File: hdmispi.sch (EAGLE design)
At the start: 3 parts

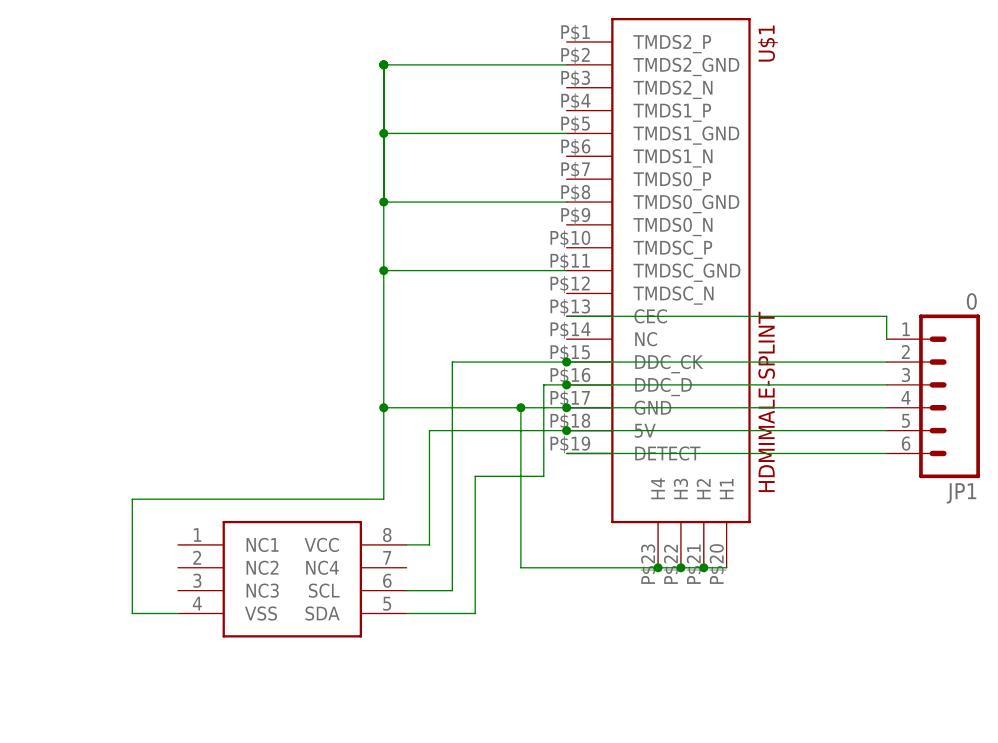
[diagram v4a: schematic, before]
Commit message: added micro hdmi header and revised board to match. note different pinout!!!
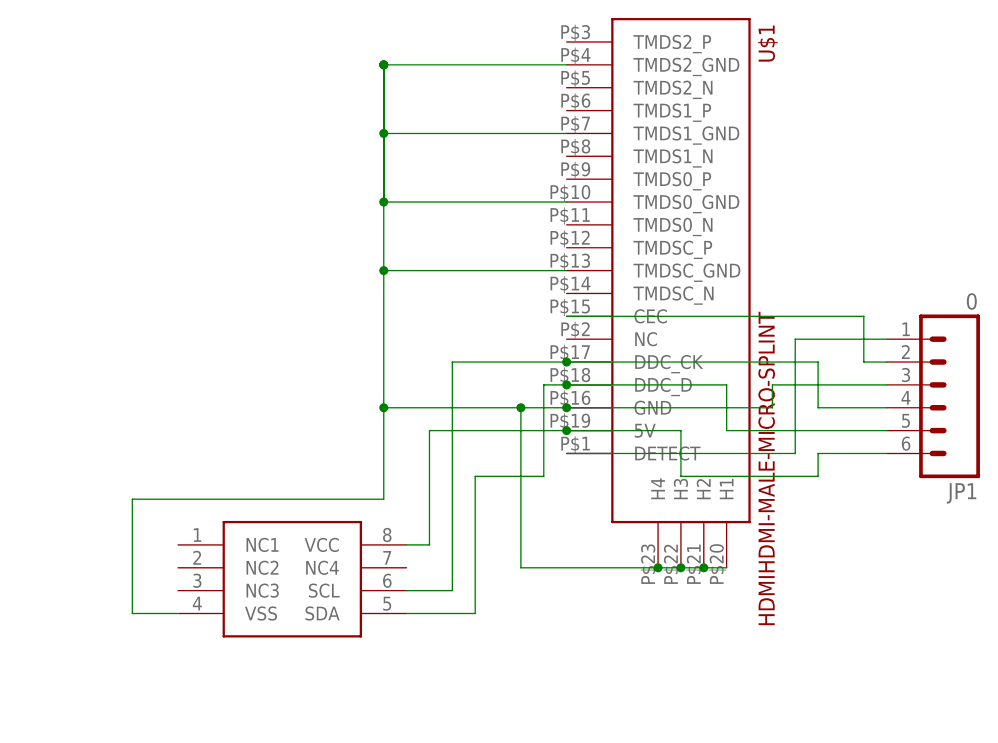
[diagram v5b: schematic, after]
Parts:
- U$1: value HDMIMALE-SPLINT -> HDMIHDMI-MALE-MICRO-SPLINT; device hdmispi:HDMIMALE-SPLINT -> hdmispi:HDMIHDMI-MALE-MICRO-SPLINT
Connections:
- removed net N$3: JP1.1, U$1.CEC
- new net N$2: JP1.2, U$1.CEC
- net 5V: now also JP1.6; no longer JP1.5
- net DDC_CK: now also JP1.4; no longer JP1.2
- net DDC_D: now also JP1.5; no longer JP1.3
- net GND: now also JP1.3; no longer JP1.4
- net N$1: now also JP1.1; no longer JP1.6
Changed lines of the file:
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@@
 <grid distance="0.1" unitdist="inch" unit="inch" style="lines" multiple="1" display="no" altdistance="0.01" altunitdist="inch" altunit="inch"/>
 <layers>
-<layer number="1" name="Top" color="4" fill="1" visible="no" active="no"/>
-<layer number="16" name="Bottom" color="1" fill="1" visible="no" active="no"/>
-<layer number="17" name="Pads" color="2" fill="1" visible="no" active="no"/>
-<layer number="18" name="Vias" color="2" fill="1" visible="no" active="no"/>
-<layer number="19" name="Unrouted" color="6" fill="1" visible="no" active="no"/>
-<layer number="20" name="Dimension" color="15" fill="1" visible="no" active="no"/>
-<layer number="21" name="tPlace" color="7" fill="1" visible="no" active="no"/>
-<layer number="22" name="bPlace" color="7" fill="1" visible="no" active="no"/>
-<layer number="23" name="tOrigins" color="15" fill="1" visible="no" active="no"/>
-<layer number="24" name="bOrigins" color="15" fill="1" visible="no" active="no"/>
-<layer number="25" name="tNames" color="7" fill="1" visible="no" active="no"/>
-<layer number="26" name="bNames" color="7" fill="1" visible="no" active="no"/>
-<layer number="27" name="tValues" color="7" fill="1" visible="no" active="no"/>
-<layer number="28" name="bValues" color="7" fill="1" visible="no" active="no"/>
+<layer number="1" name="Top" color="4" fill="1" visible="yes" active="no"/>
+<layer number="16" name="Bottom" color="1" fill="1" visible="yes" active="no"/>
+<layer number="17" name="Pads" color="2" fill="1" visible="yes" active="no"/>
+<layer number="18" name="Vias" color="2" fill="1" visible="yes" active="no"/>
+<layer number="19" name="Unrouted" color="6" fill="1" visible="yes" active="no"/>
+<layer number="20" name="Dimension" color="15" fill="1" visible="yes" active="no"/>
+<layer number="21" name="tPlace" color="7" fill="1" visible="yes" active="no"/>
+<layer number="22" name="bPlace" color="7" fill="1" visible="yes" active="no"/>
+<layer number="23" name="tOrigins" color="15" fill="1" visible="yes" active="no"/>
+<layer number="24" name="bOrigins" color="15" fill="1" visible="yes" active="no"/>
+<layer number="25" name="tNames" color="7" fill="1" visible="yes" active="no"/>
+<layer number="26" name="bNames" color="7" fill="1" visible="yes" active="no"/>
+<layer number="27" name="tValues" color="7" fill="1" visible="yes" active="no"/>
+<layer number="28" name="bValues" color="7" fill="1" visible="yes" active="no"/>
 <layer number="29" name="tStop" color="7" fill="3" visible="no" active="no"/>
 <layer number="30" name="bStop" color="7" fill="6" visible="no" active="no"/>
@@
 <layer number="35" name="tGlue" color="7" fill="4" visible="no" active="no"/>
 <layer number="36" name="bGlue" color="7" fill="5" visible="no" active="no"/>
-<layer number="37" name="tTest" color="7" fill="1" visible="no" active="no"/>
-<layer number="38" name="bTest" color="7" fill="1" visible="no" active="no"/>
+<layer number="37" name="tTest" color="7" fill="1" visible="yes" active="no"/>
+<layer number="38" name="bTest" color="7" fill="1" visible="yes" active="no"/>
 <layer number="39" name="tKeepout" color="4" fill="11" visible="no" active="no"/>
 <layer number="40" name="bKeepout" color="1" fill="11" visible="no" active="no"/>
@@
 <layer number="44" name="Drills" color="7" fill="1" visible="no" active="no"/>
 <layer number="45" name="Holes" color="7" fill="1" visible="no" active="no"/>
-<layer number="46" name="Milling" color="3" fill="1" visible="no" active="no"/>
-<layer number="47" name="Measures" color="7" fill="1" visible="no" active="no"/>
-<layer number="48" name="Document" color="7" fill="1" visible="no" active="no"/>
-<layer number="49" name="Reference" color="7" fill="1" visible="no" active="no"/>
-<layer number="50" name="dxf" color="7" fill="1" visible="no" active="no"/>
-<layer number="51" name="tDocu" color="7" fill="1" visible="no" active="no"/>
-<layer number="52" name="bDocu" color="7" fill="1" visible="no" active="no"/>
-<layer number="53" name="tGND_GNDA" color="7" fill="9" visible="no" active="no"/>
-<layer number="54" name="bGND_GNDA" color="1" fill="9" visible="no" active="no"/>
-<layer number="56" name="wert" color="7" fill="1" visible="no" active="no"/>
-<layer number="57" name="tCAD" color="7" fill="1" visible="no" active="no"/>
-<layer number="59" name="tCarbon" color="7" fill="1" visible="no" active="no"/>
-<layer number="60" name="bCarbon" color="7" fill="1" visible="no" active="no"/>
+<layer number="46" name="Milling" color="3" fill="1" visible="yes" active="no"/>
+<layer number="47" name="Measures" color="7" fill="1" visible="yes" active="no"/>
+<layer number="48" name="Document" color="7" fill="1" visible="yes" active="no"/>
+<layer number="49" name="Reference" color="7" fill="1" visible="yes" active="no"/>
+<layer number="50" name="dxf" color="7" fill="1" visible="yes" active="no"/>
+<layer number="51" name="tDocu" color="7" fill="1" visible="yes" active="no"/>
+<layer number="52" name="bDocu" color="7" fill="1" visible="yes" active="no"/>
+<layer number="53" name="tGND_GNDA" color="7" fill="9" visible="yes" active="no"/>
+<layer number="54" name="bGND_GNDA" color="1" fill="9" visible="yes" active="no"/>
+<layer number="56" name="wert" color="7" fill="1" visible="yes" active="no"/>
+<layer number="57" name="tCAD" color="7" fill="1" visible="yes" active="no"/>
+<layer number="59" name="tCarbon" color="7" fill="1" visible="yes" active="no"/>
+<layer number="60" name="bCarbon" color="7" fill="1" visible="yes" active="no"/>
 <layer number="90" name="Modules" color="5" fill="1" visible="no" active="no"/>
 <layer number="91" name="Nets" color="2" fill="1" visible="yes" active="yes"/>
@@
 </classes>
 <parts>
-<part name="U$1" library="hdmispi" deviceset="HDMI" device="MALE-SPLINT" value="HDMIMALE-SPLINT"/>
+<part name="U$1" library="hdmispi" deviceset="HDMI" device="HDMI-MALE-MICRO-SPLINT" value="HDMIHDMI-MALE-MICRO-SPLINT"/>
 <part name="U$2" library="hdmispi" deviceset="I2CEEPROM-SOIC8" device=""/>
 <part name="JP1" library="SparkFun-Connectors" deviceset="M06" device="SIP_LOCK" value="0"/>
@@
 <wire x1="35.56" y1="83.82" x2="38.1" y2="83.82" width="0.1524" layer="91"/>
 <wire x1="38.1" y1="83.82" x2="38.1" y2="96.52" width="0.1524" layer="91"/>
-<wire x1="53.34" y1="96.52" x2="88.9" y2="96.52" width="0.1524" layer="91"/>
-<pinref part="JP1" gate="G$1" pin="5"/>
+<pinref part="JP1" gate="G$1" pin="6"/>
+<wire x1="88.9" y1="93.98" x2="81.28" y2="93.98" width="0.1524" layer="91"/>
+<wire x1="81.28" y1="93.98" x2="81.28" y2="91.44" width="0.1524" layer="91"/>
+<wire x1="81.28" y1="91.44" x2="66.04" y2="91.44" width="0.1524" layer="91"/>
+<wire x1="66.04" y1="91.44" x2="66.04" y2="96.52" width="0.1524" layer="91"/>
+<wire x1="66.04" y1="96.52" x2="53.34" y2="96.52" width="0.1524" layer="91"/>
 <junction x="53.34" y="96.52"/>
 </segment>
@@
 <pinref part="U$1" gate="G$1" pin="H1"/>
 <wire x1="68.58" y1="81.28" x2="71.12" y2="81.28" width="0.1524" layer="91"/>
-<wire x1="53.34" y1="99.06" x2="88.9" y2="99.06" width="0.1524" layer="91"/>
-<pinref part="JP1" gate="G$1" pin="4"/>
+<pinref part="JP1" gate="G$1" pin="3"/>
+<wire x1="88.9" y1="101.6" x2="76.2" y2="101.6" width="0.1524" layer="91"/>
+<wire x1="76.2" y1="101.6" x2="76.2" y2="99.06" width="0.1524" layer="91"/>
+<wire x1="76.2" y1="99.06" x2="53.34" y2="99.06" width="0.1524" layer="91"/>
 <junction x="53.34" y="99.06"/>
 </segment>
@@
 <wire x1="35.56" y1="76.2" x2="43.18" y2="76.2" width="0.1524" layer="91"/>
 <wire x1="43.18" y1="76.2" x2="43.18" y2="91.44" width="0.1524" layer="91"/>
-<wire x1="53.34" y1="101.6" x2="88.9" y2="101.6" width="0.1524" layer="91"/>
-<pinref part="JP1" gate="G$1" pin="3"/>
+<wire x1="53.34" y1="101.6" x2="71.12" y2="101.6" width="0.1524" layer="91"/>
+<wire x1="71.12" y1="101.6" x2="71.12" y2="96.52" width="0.1524" layer="91"/>
+<pinref part="JP1" gate="G$1" pin="5"/>
+<wire x1="71.12" y1="96.52" x2="88.9" y2="96.52" width="0.1524" layer="91"/>
 <junction x="53.34" y="101.6"/>
 </segment>
@@
 <wire x1="35.56" y1="78.74" x2="40.64" y2="78.74" width="0.1524" layer="91"/>
 <wire x1="40.64" y1="78.74" x2="40.64" y2="104.14" width="0.1524" layer="91"/>
-<wire x1="88.9" y1="104.14" x2="53.34" y2="104.14" width="0.1524" layer="91"/>
+<pinref part="JP1" gate="G$1" pin="4"/>
+<wire x1="88.9" y1="99.06" x2="81.28" y2="99.06" width="0.1524" layer="91"/>
+<wire x1="81.28" y1="99.06" x2="81.28" y2="104.14" width="0.1524" layer="91"/>
+<wire x1="81.28" y1="104.14" x2="53.34" y2="104.14" width="0.1524" layer="91"/>
+<junction x="53.34" y="104.14"/>
+</segment>
+</net>
+<net name="N$1" class="0">
+<segment>
+<pinref part="U$1" gate="G$1" pin="DETECT"/>
+<wire x1="53.34" y1="93.98" x2="78.74" y2="93.98" width="0.1524" layer="91"/>
+<wire x1="78.74" y1="93.98" x2="78.74" y2="106.68" width="0.1524" layer="91"/>
+<pinref part="JP1" gate="G$1" pin="1"/>
+<wire x1="78.74" y1="106.68" x2="88.9" y2="106.68" width="0.1524" layer="91"/>
+</segment>
+</net>
+<net name="N$2" class="0">
+<segment>
+<pinref part="U$1" gate="G$1" pin="CEC"/>
+<wire x1="53.34" y1="109.22" x2="86.36" y2="109.22" width="0.1524" layer="91"/>
+<wire x1="86.36" y1="109.22" x2="86.36" y2="104.14" width="0.1524" layer="91"/>
 <pinref part="JP1" gate="G$1" pin="2"/>
-<junction x="53.34" y="104.14"/>
-</segment>
-</net>
-<net name="N$1" class="0">
-<segment>
-<pinref part="U$1" gate="G$1" pin="DETECT"/>
-<wire x1="53.34" y1="93.98" x2="88.9" y2="93.98" width="0.1524" layer="91"/>
-<pinref part="JP1" gate="G$1" pin="6"/>
-</segment>
-</net>
-<net name="N$3" class="0">
-<segment>
-<wire x1="53.34" y1="109.22" x2="88.9" y2="109.22" width="0.1524" layer="91"/>
-<pinref part="JP1" gate="G$1" pin="1"/>
-<wire x1="88.9" y1="109.22" x2="88.9" y2="106.68" width="0.1524" layer="91"/>
-<pinref part="U$1" gate="G$1" pin="CEC"/>
-</segment>
-</net>
+<wire x1="86.36" y1="104.14" x2="88.9" y2="104.14" width="0.1524" layer="91"/>
+</segment>
+</net>
